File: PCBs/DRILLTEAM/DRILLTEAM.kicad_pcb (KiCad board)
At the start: 2 copper layers, 100 x 100 mm, 84 parts, among them J10 Conn_01x04, J11 Conn_01x08, J12 Conn_01x04, J13 TYPE-C-31-M-12, J2 Conn_01x02, J3 Conn_01x03, J4 Conn_01x03, J5 Conn_01x04, J6 Conn_01x04, J7 Conn_01x02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

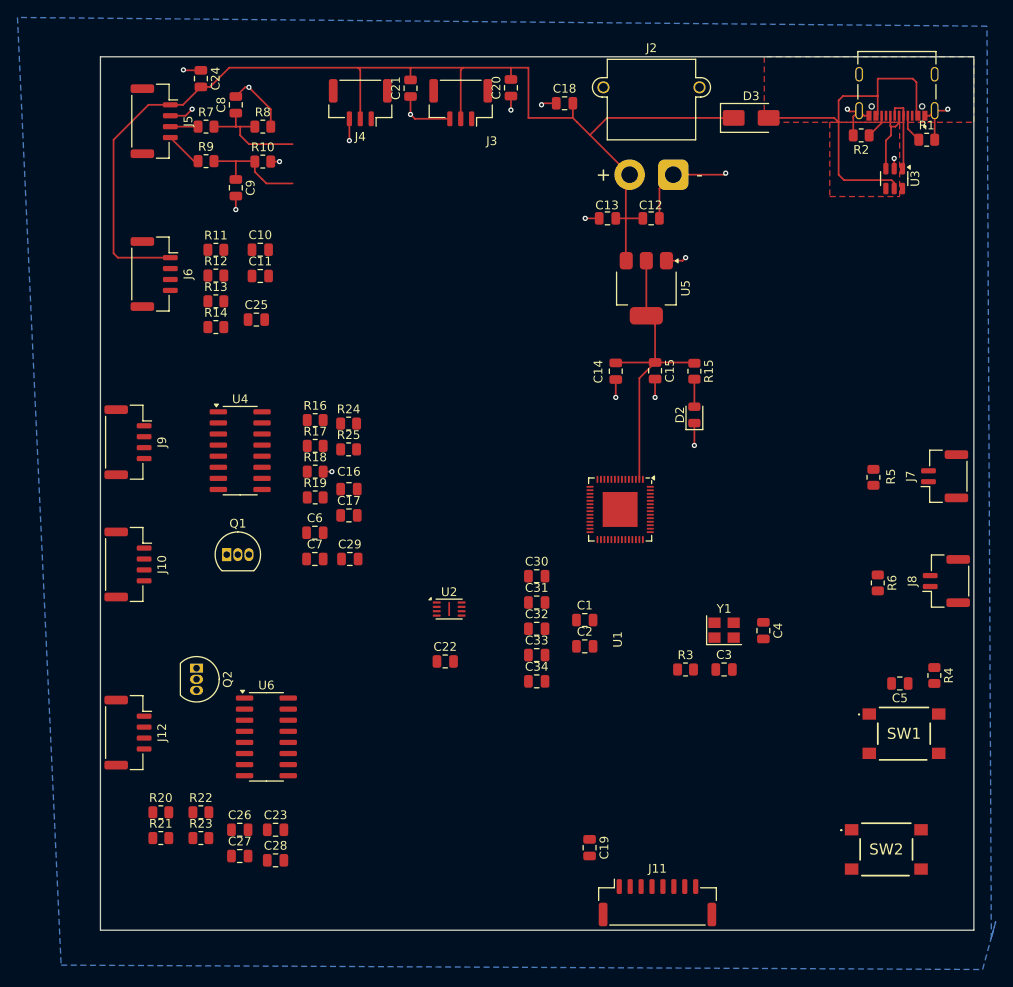
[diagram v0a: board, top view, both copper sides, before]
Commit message: Finished PCB sub mounting holes and fillet
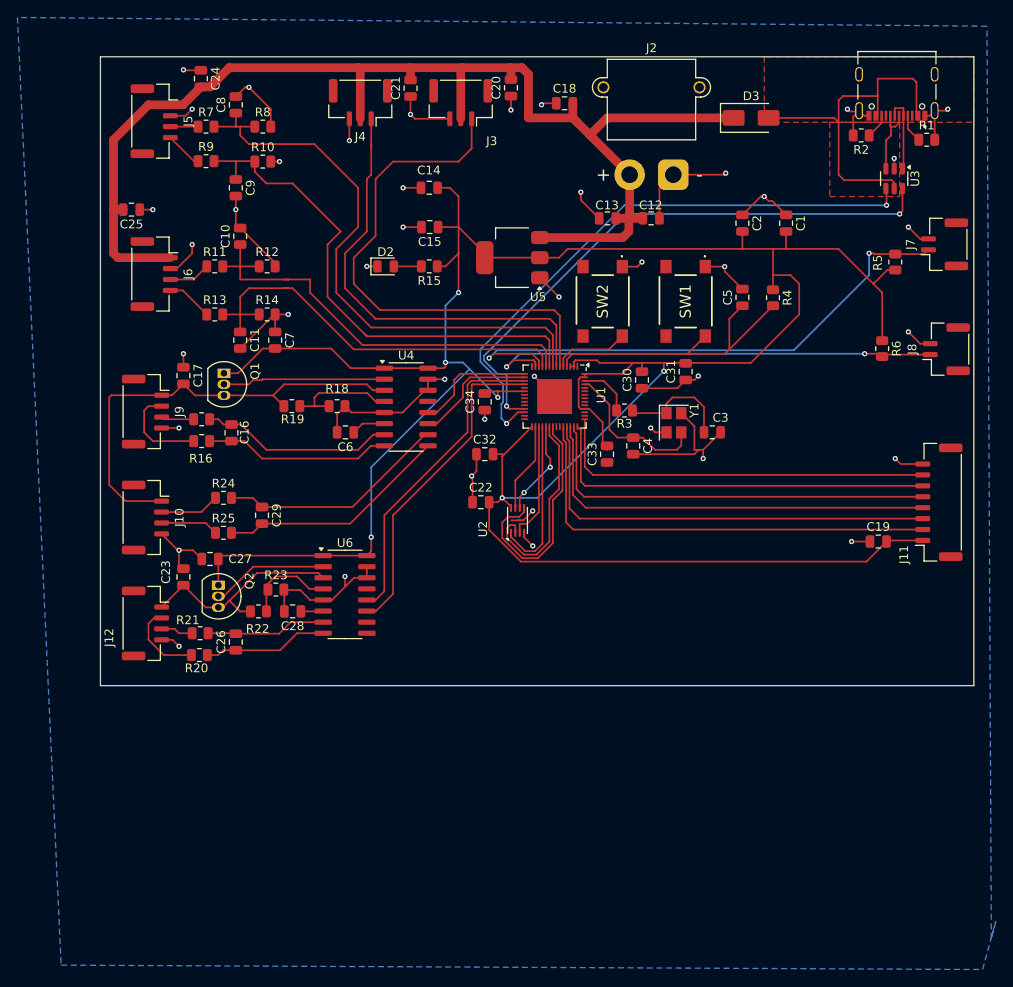
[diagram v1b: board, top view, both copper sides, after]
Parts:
- moved SW2 70.7 mm to (86.5, 50.0), turned to -90 degrees
- moved J11 56.0 mm to (125.0, 73.0), turned to 90 degrees
- moved SW1 55.5 mm to (96.0, 50.0), turned to -90 degrees
- moved C2 51.7 mm to (102.5, 41.0), turned to -90 degrees
- moved C1 51.0 mm to (107.5, 41.0), turned to -90 degrees
- moved C19 48.2 mm to (118.0, 77.5), turned to 0 degrees
- moved C5 47.7 mm to (102.5, 49.5), turned to 90 degrees
- moved R4 47.0 mm to (106.0, 49.6)
- moved D2 39.2 mm to (61.6, 46.0), turned to 0 degrees
- moved C27 34.2 mm to (41.5, 79.5)
- moved R15 32.6 mm to (66.7, 46.0), turned to 180 degrees
- moved C34 32.6 mm to (73.0, 61.5), turned to 90 degrees
- moved C31 31.5 mm to (96.0, 58.0), turned to 90 degrees
- moved C23 30.8 mm to (38.5, 81.5), turned to -90 degrees
- moved C15 30.6 mm to (66.7, 41.5), turned to 180 degrees
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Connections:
- U1 pad 14: /LC1CLK -> unconnected-(U1-GPIO9-Pad14)
- U1 pad 16: /LC2CLK -> /LC1CLK
- U1 pad 18: /LC3CLK -> /LC2CLK
- U1 pad 19: /LC3DT -> unconnected-(U1-GPIO14-Pad19)
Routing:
- net +3.3V: track 26.2 -> 333.7 mm, vias 0 -> 6
- net GND: track 64.5 -> 202.6 mm, vias 19 -> 42
- net Net-(U1-GPIO20/USB_D+): track 0.00 -> 67.8 mm, vias 0 -> 2
- net Net-(U1-GPIO19/USB_D-): track 0.00 -> 67.0 mm, vias 0 -> 2
- net /LS1: track 0.00 -> 63.9 mm, vias 0 -> 2
- net /Servo1: track 0.00 -> 59.8 mm
- net /LS2: track 0.00 -> 53.5 mm, vias 0 -> 2
- net /ENC1A: track 13.6 -> 66.7 mm
- net /M1P: track 0.00 -> 52.3 mm
- net Net-(J10-Pin_1): track 0.00 -> 52.0 mm
- net /Servo2: track 0.00 -> 51.8 mm
- net /M1IA: track 0.00 -> 50.4 mm
- net /ENC2A: track 0.00 -> 49.8 mm
- net /M1IB: track 0.00 -> 48.6 mm
- net /ENC2B: track 0.00 -> 48.2 mm
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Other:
- board size 100 x 100 mm -> 100 x 72 mm

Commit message: Small changes to drill PCB
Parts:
- added G***: LOGO, footprints:IPRL_31mm, F.Cu at (96.9, 80.2)
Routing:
- net +3.3V: track 333.7 -> 330.6 mm
- net GND: track 202.6 -> 204.8 mm, vias 42 -> 43
- net Net-(U1-GPIO19/USB_D-): track 67.0 -> 66.4 mm

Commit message: Finished Drill PCB
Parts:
- added H1: MountingHole, MountingHole:MountingHole_3.2mm_M3, F.Cu at (124.0, 88.0)
- added H2: MountingHole, MountingHole:MountingHole_3.2mm_M3, F.Cu at (67.5, 88.0)
- added H3: MountingHole, MountingHole:MountingHole_3.2mm_M3, F.Cu at (78.5, 35.0)
- Encoder 1: renamed from J5; value Conn_01x04 -> Encoder 2
- Encoder 2: renamed from J6; value Conn_01x04 -> Encoder 1
- Limit Switch 1: renamed from J8
- Limit Switch 2: renamed from J7
- Load Cell 1: renamed from J9; value Conn_01x04 -> Load Cell 1
- Load Cell 2: renamed from J10; value Conn_01x04 -> Load Cell 2
- Load Cell 3: renamed from J12; value Conn_01x04 -> Load Cell 3
- Motor Driver: renamed from J11
- Power In: renamed from J2
- Servo 1: renamed from J4
- Servo 2: renamed from J3
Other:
- outline, holes or cut-outs redrawn
- board text added: "Any issues, ask Eren S"
- board text added: "Drill Board"

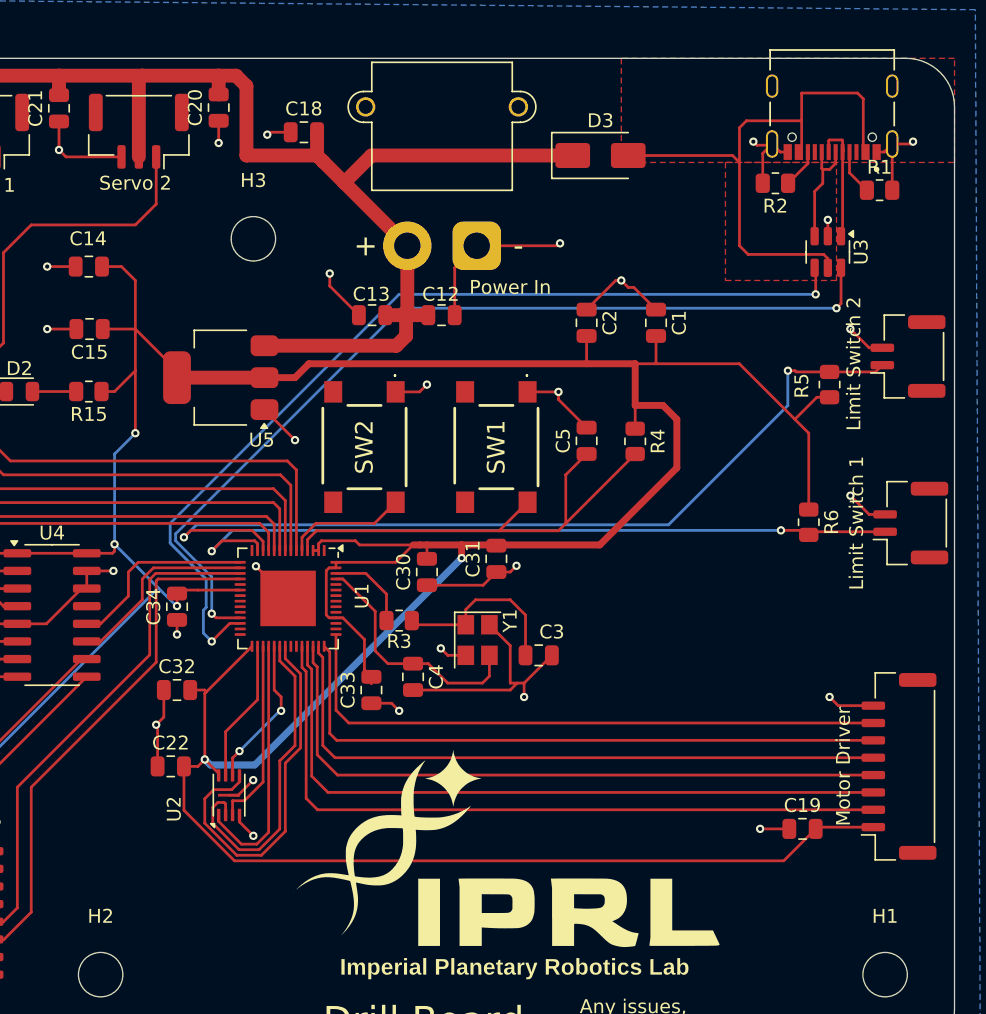
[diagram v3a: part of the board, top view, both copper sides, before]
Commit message: Manufacturing data created + added names to PCBs.
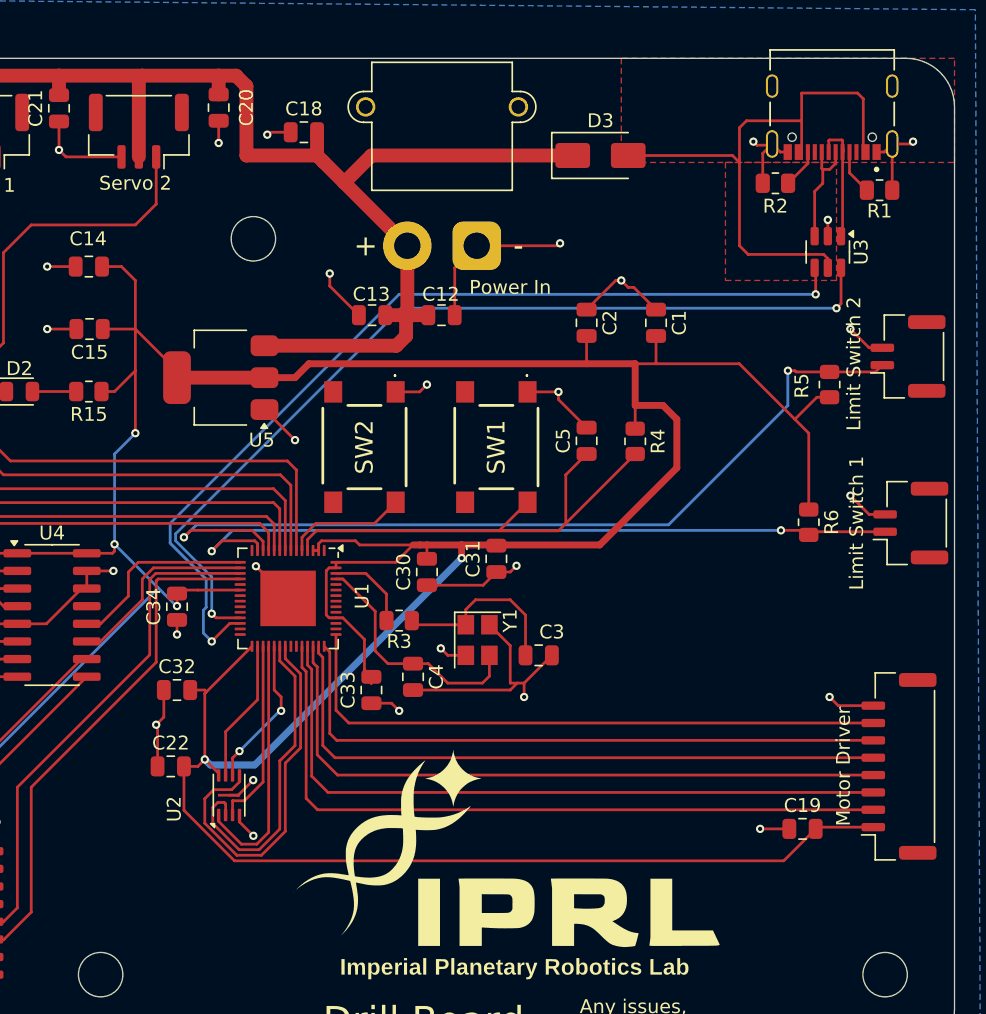
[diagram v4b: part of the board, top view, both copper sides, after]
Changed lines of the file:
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@@
 			(plotinvisibletext no)
 			(sketchpadsonfab no)
-			(subtractmaskfromsilk no)
+			(subtractmaskfromsilk yes)
 			(outputformat 1)
 			(mirror no)
-			(drillshape 1)
+			(drillshape 0)
 			(scaleselection 1)
-			(outputdirectory "")
+			(outputdirectory "output/")
 		)
 	)
@@
 			(at 0 -4.2 0)
 			(layer "F.SilkS")
+			(hide yes)
 			(effects
 				(font
@@
 			(at 0 -4.2 0)
 			(layer "F.SilkS")
+			(hide yes)
 			(effects
 				(font
@@
 		(tags "resistor")
 		(property "Reference" "R1"
-			(at 0 -1.65 0)
+			(at 0 1.5 0)
 			(layer "F.SilkS")
 			(effects
@@
 			(at 0 -4.2 0)
 			(layer "F.SilkS")
+			(hide yes)
 			(effects
 				(font
@@
 		(tags "capacitor")
 		(property "Reference" "C20"
-			(at 0 -1.68 90)
+			(at 0 2 90)
 			(layer "F.SilkS")
 			(effects
